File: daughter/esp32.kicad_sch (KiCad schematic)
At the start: 15 parts, among them SW2 SW_Push, U1 ESP32-C3, Y1 40M

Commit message: Common PSU
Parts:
- gave numbers to parts that had none: 5
- renumbered C5 to C10, C6 to C11, C8 to C12, C9 to C13, C7 to C14, C4 to C9, U1 to U3
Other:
- moved on the sheet: C14
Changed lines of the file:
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@@
 	(wire
 		(pts
-			(xy 152.4 68.58) (xy 173.99 68.58)
+			(xy 153.67 68.58) (xy 173.99 68.58)
 		)
 		(stroke
@@
 	(wire
 		(pts
-			(xy 101.6 113.03) (xy 101.6 106.68)
+			(xy 146.05 68.58) (xy 144.78 68.58)
 		)
 		(stroke
@@
 	(wire
 		(pts
-			(xy 144.78 68.58) (xy 144.78 72.39)
+			(xy 101.6 113.03) (xy 101.6 106.68)
 		)
 		(stroke
@@
 		(pts
 			(xy 97.79 71.12) (xy 129.54 71.12)
+		)
+		(stroke
+			(width 0)
+			(type default)
+		)
+	)
+	(wire
+		(pts
+			(xy 144.78 68.58) (xy 144.78 72.39)
 		)
 		(stroke
@@
 	(symbol
 		(lib_id "Device:C")
-		(at 148.59 68.58 90)
-		(unit 1)
-		(exclude_from_sim no)
-		(in_bom yes)
-		(on_board yes)
-		(dnp no)
-		(property "Reference" "C7"
-			(at 147.32 67.564 90)
+		(at 149.86 68.58 90)
+		(unit 1)
+		(exclude_from_sim no)
+		(in_bom yes)
+		(on_board yes)
+		(dnp no)
+		(property "Reference" "C14"
+			(at 148.59 67.564 90)
 			(effects
 				(font
@@
 		)
 		(property "Value" "100n"
-			(at 154.686 67.31 90)
-			(effects
-				(font
-					(size 1.27 1.27)
-				)
-				(justify left)
-			)
-		)
-		(property "Footprint" ""
-			(at 152.4 67.6148 0)
+			(at 155.956 67.31 90)
+			(effects
+				(font
+					(size 1.27 1.27)
+				)
+				(justify left)
+			)
+		)
+		(property "Footprint" ""
+			(at 153.67 67.6148 0)
 			(effects
 				(font
@@
 		)
 		(property "Datasheet" "~"
-			(at 148.59 68.58 0)
+			(at 149.86 68.58 0)
 			(effects
 				(font
@@
 		)
 		(property "Description" "Unpolarized capacitor"
-			(at 148.59 68.58 0)
+			(at 149.86 68.58 0)
 			(effects
 				(font
@@
 			(project "daughter"
 				(path "/9e050361-84ba-4b41-8bc1-d0f304e5538b/289ab7b1-b3e2-41d0-8980-3ae1a9541378"
-					(reference "C7")
+					(reference "C14")
 					(unit 1)
 				)
@@
 		(on_board yes)
 		(dnp no)
-		(property "Reference" "SW?"
+		(property "Reference" "SW3"
 			(at 171.45 85.09 0)
 			(effects
@@
 			(project "daughter"
 				(path "/9e050361-84ba-4b41-8bc1-d0f304e5538b/289ab7b1-b3e2-41d0-8980-3ae1a9541378"
-					(reference "SW?")
+					(reference "SW3")
 					(unit 1)
 				)
@@
 		(on_board yes)
 		(dnp no)
-		(property "Reference" "R?"
+		(property "Reference" "R1"
 			(at 169.164 73.914 0)
 			(effects
@@
 			(project "daughter"
 				(path "/9e050361-84ba-4b41-8bc1-d0f304e5538b/289ab7b1-b3e2-41d0-8980-3ae1a9541378"
-					(reference "R?")
+					(reference "R1")
 					(unit 1)
 				)
@@
 		(on_board yes)
 		(dnp no)
-		(property "Reference" "C8"
+		(property "Reference" "C12"
 			(at 128.524 61.468 0)
 			(effects
@@
 			(project "daughter"
 				(path "/9e050361-84ba-4b41-8bc1-d0f304e5538b/289ab7b1-b3e2-41d0-8980-3ae1a9541378"
-					(reference "C8")
+					(reference "C12")
 					(unit 1)
 				)
@@
 		(on_board yes)
 		(dnp no)
-		(property "Reference" "C?"
+		(property "Reference" "C15"
 			(at 98.806 114.046 0)
 			(effects
@@
 			(project "daughter"
 				(path "/9e050361-84ba-4b41-8bc1-d0f304e5538b/289ab7b1-b3e2-41d0-8980-3ae1a9541378"
-					(reference "C?")
+					(reference "C15")
 					(unit 1)
 				)
@@
 		(on_board yes)
 		(dnp no)
-		(property "Reference" "C6"
+		(property "Reference" "C11"
 			(at 123.444 61.468 0)
 			(effects
@@
 			(project "daughter"
 				(path "/9e050361-84ba-4b41-8bc1-d0f304e5538b/289ab7b1-b3e2-41d0-8980-3ae1a9541378"
-					(reference "C6")
+					(reference "C11")
 					(unit 1)
 				)
@@
 		(on_board yes)
 		(dnp no)
-		(property "Reference" "C4"
+		(property "Reference" "C9"
 			(at 113.284 61.468 0)
 			(effects
@@
 			(project "daughter"
 				(path "/9e050361-84ba-4b41-8bc1-d0f304e5538b/289ab7b1-b3e2-41d0-8980-3ae1a9541378"
-					(reference "C4")
+					(reference "C9")
 					(unit 1)
 				)
@@
 		(on_board yes)
 		(dnp no)
-		(property "Reference" "U1"
+		(property "Reference" "U3"
 			(at 138.938 96.266 0)
 			(effects
@@
 			(project "daughter"
 				(path "/9e050361-84ba-4b41-8bc1-d0f304e5538b/289ab7b1-b3e2-41d0-8980-3ae1a9541378"
-					(reference "U1")
+					(reference "U3")
 					(unit 1)
 				)
@@
 		(on_board yes)
 		(dnp no)
-		(property "Reference" "C?"
+		(property "Reference" "C16"
 			(at 111.76 114.046 0)
 			(effects
@@
 			(project "daughter"
 				(path "/9e050361-84ba-4b41-8bc1-d0f304e5538b/289ab7b1-b3e2-41d0-8980-3ae1a9541378"
-					(reference "C?")
+					(reference "C16")
 					(unit 1)
 				)
@@
 		(on_board yes)
 		(dnp no)
-		(property "Reference" "C9"
+		(property "Reference" "C13"
 			(at 133.604 61.468 0)
 			(effects
@@
 			(project "daughter"
 				(path "/9e050361-84ba-4b41-8bc1-d0f304e5538b/289ab7b1-b3e2-41d0-8980-3ae1a9541378"
-					(reference "C9")
+					(reference "C13")
 					(unit 1)
 				)
@@
 		(on_board yes)
 		(dnp no)
-		(property "Reference" "C5"
+		(property "Reference" "C10"
 			(at 118.364 61.468 0)
 			(effects
@@
 			(project "daughter"
 				(path "/9e050361-84ba-4b41-8bc1-d0f304e5538b/289ab7b1-b3e2-41d0-8980-3ae1a9541378"
-					(reference "C5")
+					(reference "C10")
 					(unit 1)
 				)
@@
 		(on_board yes)
 		(dnp no)
-		(property "Reference" "C?"
+		(property "Reference" "C8"
 			(at 108.204 61.468 0)
 			(effects
@@
 			(project "daughter"
 				(path "/9e050361-84ba-4b41-8bc1-d0f304e5538b/289ab7b1-b3e2-41d0-8980-3ae1a9541378"
-					(reference "C?")
-					(unit 1)
-				)
+					(reference "C8")
+					(unit 1)
+				)

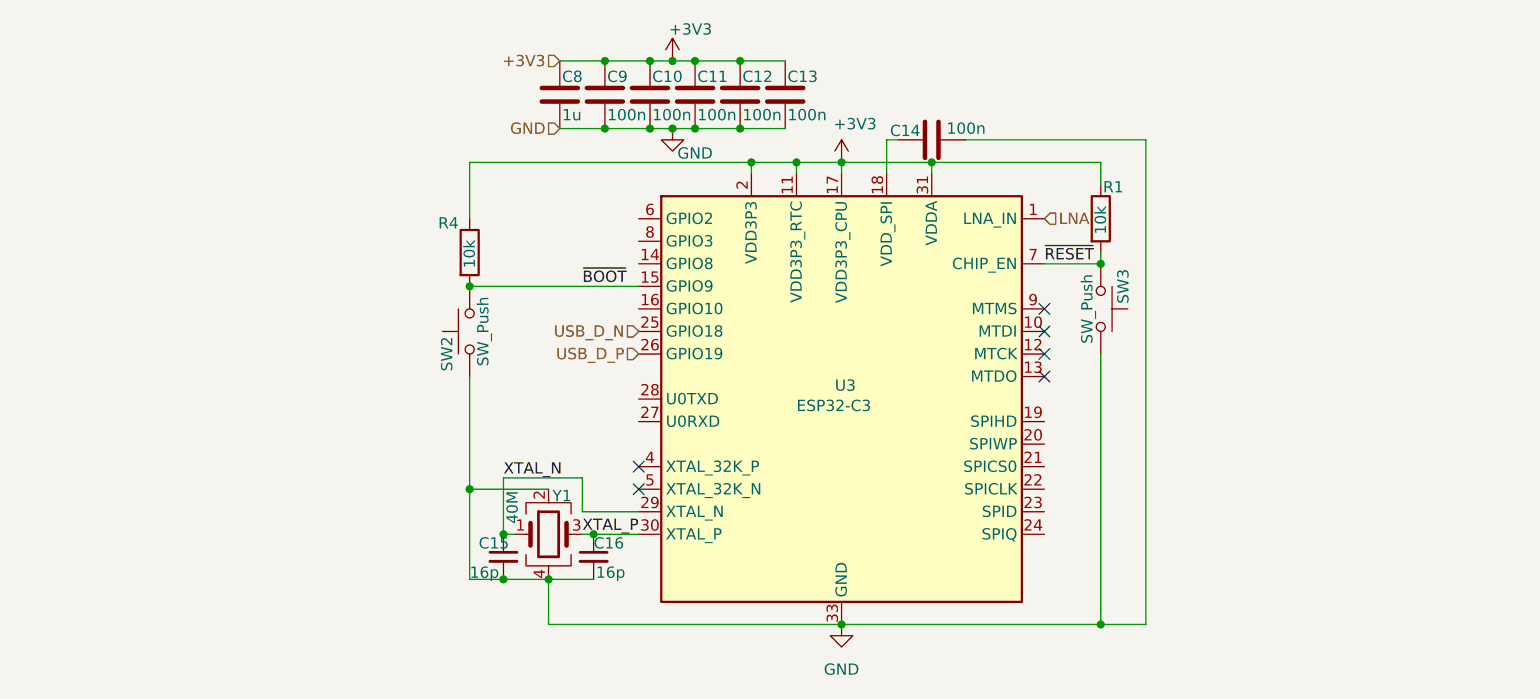
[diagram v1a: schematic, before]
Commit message: Component selection: power relay (needs MOSFET), placeholder pressure sensor.
Pressure sensor placeholder goes underwater, am stuck with finding one that doesn't that is ALSO on Sierra portal.
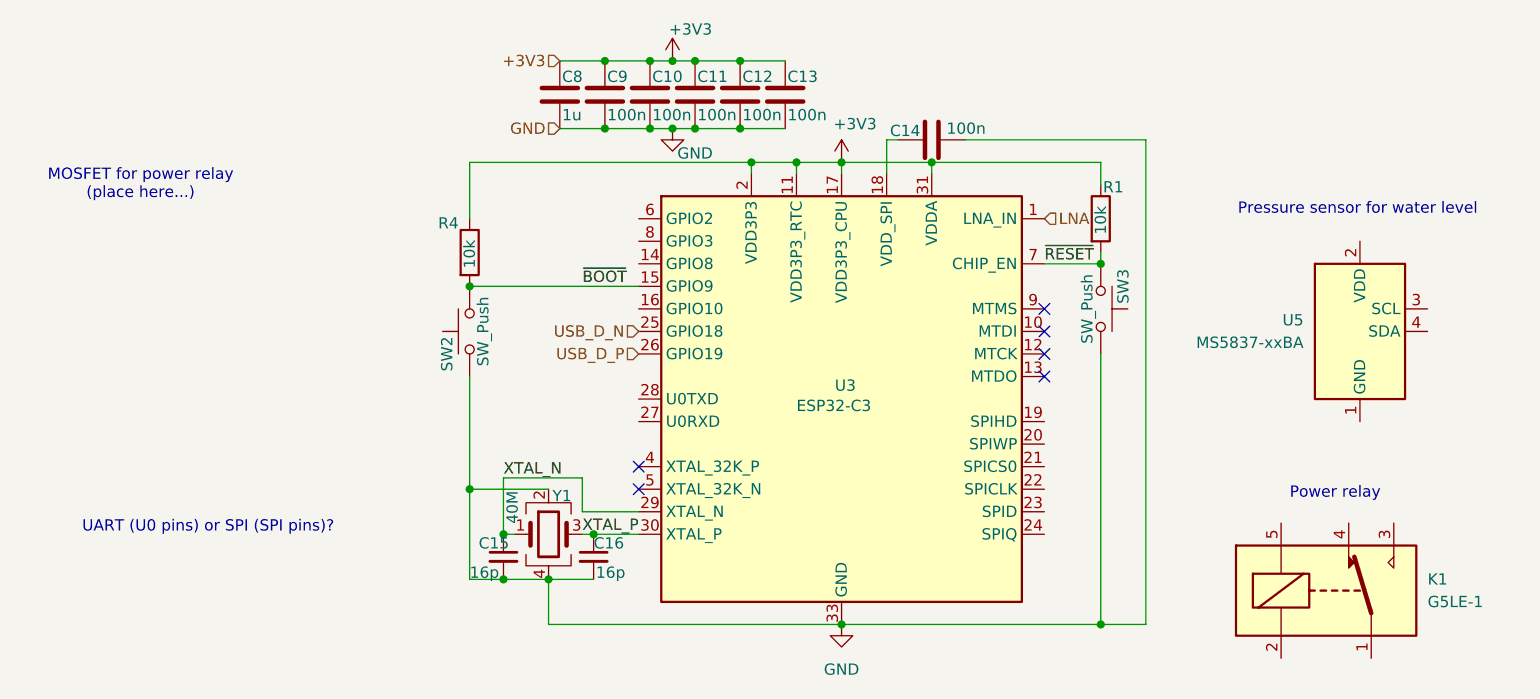
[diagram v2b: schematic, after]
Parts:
- added K1: G5LE-1, Relay_THT:Relay_SPDT_Omron-G5LE-1, symbol Relay:G5LE-1
- added U5: MS5837-xxBA, Sensor_Pressure:TE_MS5837-xxBA, symbol Sensor_Pressure:MS5837-xxBA
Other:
- note added: "MOSFET for power relay (place here...)"
- note added: "Power relay"
- note added: "Pressure sensor for water level"
- note added: "UART (U0 pins) or SPI (SPI pins)?"
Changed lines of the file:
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@@
+		)
+	)
+	(text "MOSFET for power relay\n(place here...)"
+		(exclude_from_sim no)
+		(at 60.706 73.66 0)
+		(effects
+			(font
+				(size 1.27 1.27)
+			)
+		)
+	)
+	(text "UART (U0 pins) or SPI (SPI pins)?"
+		(exclude_from_sim no)
+		(at 68.326 112.268 0)
+		(effects
+			(font
+				(size 1.27 1.27)
+			)
+		)
+	)
+	(text "Pressure sensor for water level"
+		(exclude_from_sim no)
+		(at 197.866 76.454 0)
+		(effects
+			(font
+				(size 1.27 1.27)
+			)
+		)
+	)
+	(text "Power relay"
+		(exclude_from_sim no)
+		(at 195.326 108.458 0)
+		(effects
+			(font
+				(size 1.27 1.27)
+			)
 		)
 	)
@@
 	)
 	(symbol
+		(lib_id "Sensor_Pressure:MS5837-xxBA")
+		(at 198.12 90.17 0)
+		(unit 1)
+		(exclude_from_sim no)
+		(in_bom yes)
+		(on_board yes)
+		(dnp no)
+		(fields_autoplaced yes)
+		(property "Reference" "U5"
+			(at 191.77 88.8999 0)
+			(effects
+				(font
+					(size 1.27 1.27)
+				)
+				(justify right)
+			)
+		)
+		(property "Value" "MS5837-xxBA"
+			(at 191.77 91.4399 0)
+			(effects
+				(font
+					(size 1.27 1.27)
+				)
+				(justify right)
+			)
+		)
+		(property "Footprint" "Sensor_Pressure:TE_MS5837-xxBA"
+			(at 198.12 90.17 0)
+			(effects
+				(font
+					(size 1.27 1.27)
+				)
+				(hide yes)
+			)
+		)
+		(property "Datasheet" "https://www.te.com/commerce/DocumentDelivery/DDEController?Action=showdoc&DocId=Data+Sheet%7FMS5837-30BA%7FB1%7Fpdf%7FEnglish%7FENG_DS_MS5837-30BA_B1.pdf%7FCAT-BLPS0017"
+			(at 198.12 92.71 0)
+			(effects
+				(font
+					(size 1.27 1.27)
+				)
+				(hide yes)
+			)
+		)
+		(property "Description" "Ultra-small, gel-filled, pressure sensor with stainless steel cap"
+			(at 198.12 90.17 0)
+			(effects
+				(font
+					(size 1.27 1.27)
+				)
+				(hide yes)
+			)
+		)
+		(pin "1"
+		)
+		(pin "2"
+		)
+		(pin "3"
+		)
+		(pin "4"
+		)
+		(instances
+			(project "daughter"
+				(path "/9e050361-84ba-4b41-8bc1-d0f304e5538b/289ab7b1-b3e2-41d0-8980-3ae1a9541378"
+					(reference "U5")
+					(unit 1)
+				)
+			)
+		)
+	)
+	(symbol
 		(lib_id "Switch:SW_Push")
 		(at 168.91 87.63 270)
@@
 					(unit 1)
 				)
+			)
+		)
+	)
+	(symbol
+		(lib_id "Relay:G5LE-1")
+		(at 194.31 119.38 0)
+		(unit 1)
+		(exclude_from_sim no)
+		(in_bom yes)
+		(on_board yes)
+		(dnp no)
+		(fields_autoplaced yes)
+		(property "Reference" "K1"
+			(at 205.74 118.1099 0)
+			(effects
+				(font
+					(size 1.27 1.27)
+				)
+				(justify left)
+			)
+		)
+		(property "Value" "G5LE-1"
+			(at 205.74 120.6499 0)
+			(effects
+				(font
+					(size 1.27 1.27)
+				)
+				(justify left)
+			)
+		)
+		(property "Footprint" "Relay_THT:Relay_SPDT_Omron-G5LE-1"
+			(at 205.74 120.65 0)
+			(effects
+				(font
+					(size 1.27 1.27)
+				)
+				(justify left)
+				(hide yes)
+			)
+		)
+		(property "Datasheet" "http://www.omron.com/ecb/products/pdf/en-g5le.pdf"
+			(at 194.31 119.38 0)
+			(effects
+				(font
+					(size 1.27 1.27)
+				)
+				(hide yes)
+			)
+		)
+		(property "Description" "Omron G5LE relay, Miniature Single Pole, SPDT, 10A"
+			(at 194.31 119.38 0)
+			(effects
+				(font
+					(size 1.27 1.27)
+				)
+				(hide yes)
+			)
+		)
+		(pin "2"
+		)
+		(pin "3"
+		)
+		(pin "4"
+		)
+		(pin "5"
+		)
+		(pin "1"
+		)
+		(instances
+			(project "daughter"
+				(path "/9e050361-84ba-4b41-8bc1-d0f304e5538b/289ab7b1-b3e2-41d0-8980-3ae1a9541378"
+					(reference "K1")
+					(unit 1)
+				)
